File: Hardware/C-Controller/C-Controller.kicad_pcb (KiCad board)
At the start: 2 copper layers, 23 x 20 mm, 21 parts, among them J1 Conn_01x02, J2 Conn_01x04, J3 Conn_01x06, J4 Conn_01x07, J5 Conn_01x05, U1 STM32L031K6Tx

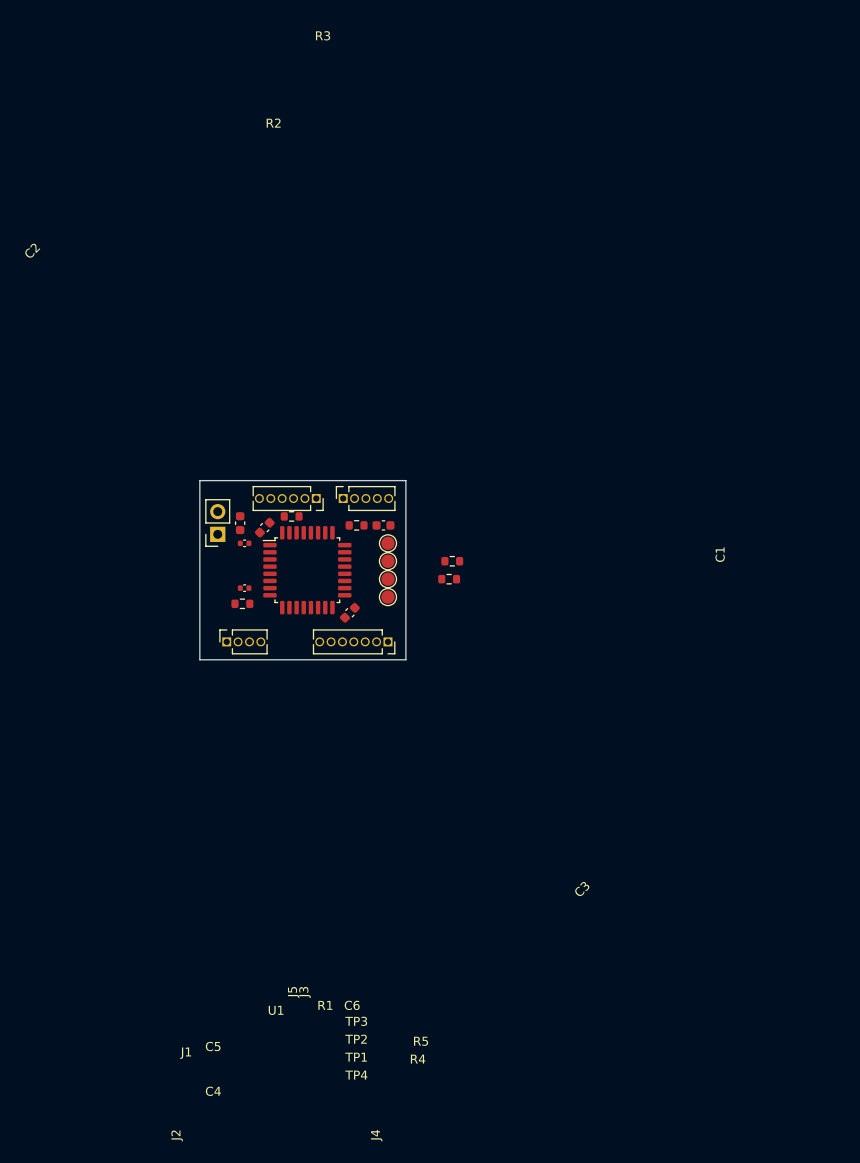
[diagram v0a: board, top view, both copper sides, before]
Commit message: 1mm pitch headers
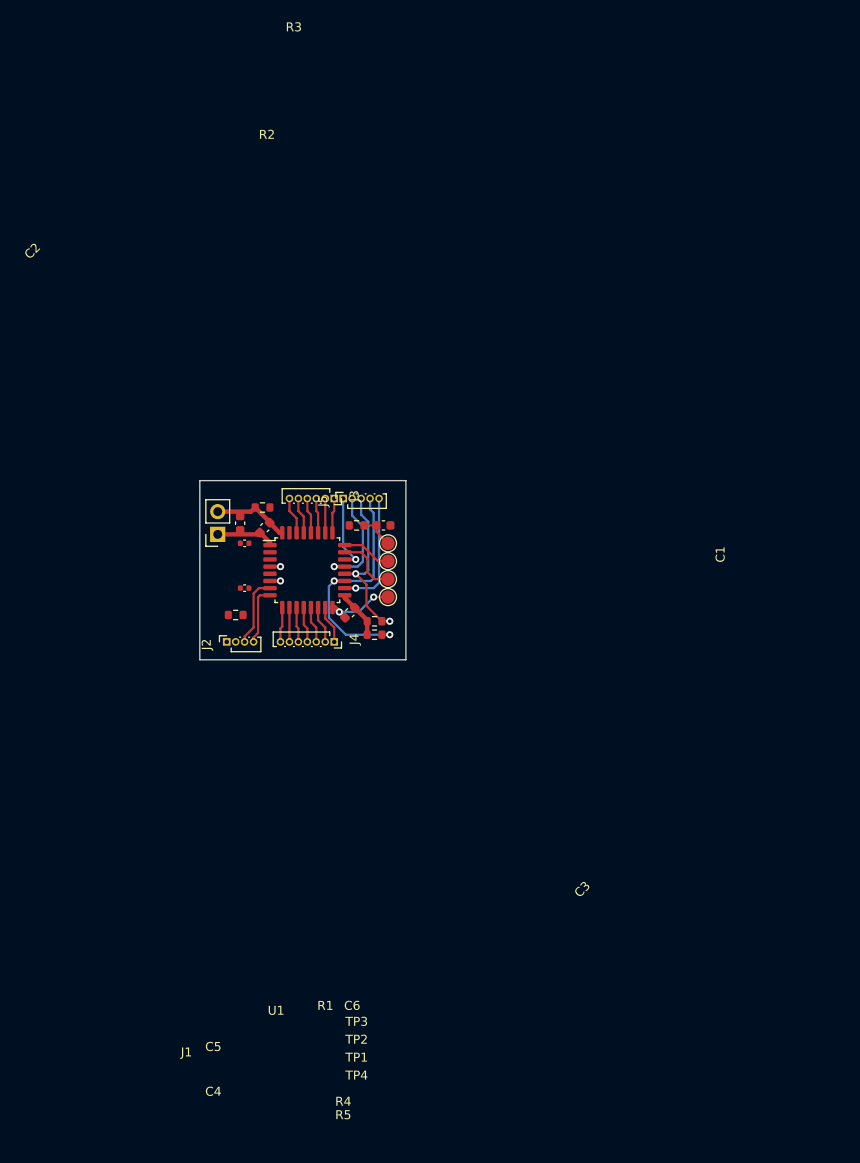
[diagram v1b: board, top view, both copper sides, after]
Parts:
- J2: footprint Connector_PinSocket_1.27mm:PinSocket_1x04_P1.27mm_Vertical -> Connector_PinSocket_1.00mm:PinSocket_1x04_P1.00mm_Vertical
- J3: footprint Connector_PinSocket_1.27mm:PinSocket_1x06_P1.27mm_Vertical -> Connector_PinSocket_1.00mm:PinSocket_1x06_P1.00mm_Vertical
- J4: footprint Connector_PinSocket_1.27mm:PinSocket_1x07_P1.27mm_Vertical -> Connector_PinSocket_1.00mm:PinSocket_1x07_P1.00mm_Vertical
- J5: footprint Connector_PinSocket_1.27mm:PinSocket_1x05_P1.27mm_Vertical -> Connector_PinSocket_1.00mm:PinSocket_1x05_P1.00mm_Vertical
- moved R5 11.9 mm to (127.5, 87.2)
- moved R4 9.56 mm to (127.5, 85.7)
- moved J4 6.00 mm to (123.0, 88.0)
- moved R3 3.40 mm to (115.0, 73.0)
- moved J3 2.00 mm to (123.0, 72.0)
- moved R2 1.46 mm to (112.0, 85.0)
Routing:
- net I2D1_SCL: track 0.00 -> 27.6 mm, vias 0 -> 2
- net I2C1_SDA: track 0.00 -> 18.5 mm, vias 0 -> 2
- net GND: track 0.00 -> 17.6 mm, vias 0 -> 2
- net PA8: track 0.00 -> 13.5 mm, vias 0 -> 1
- net PA11: track 0.00 -> 12.1 mm, vias 0 -> 1
- net +3V3: track 0.00 -> 11.9 mm
- net PA12: track 0.00 -> 8.60 mm, vias 0 -> 1
- net PA1: track 0.00 -> 7.89 mm
- net SYS_SWDIO: track 0.00 -> 6.95 mm
- net USART2_TX: track 0.00 -> 6.61 mm
- net SYS_SWCLK: track 0.00 -> 5.57 mm
- net RESET: track 0.00 -> 5.10 mm, vias 0 -> 1
- net PB1: track 0.00 -> 4.30 mm
- net PB7: track 0.00 -> 4.16 mm
- net PB0: track 0.00 -> 4.16 mm
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
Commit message: smaller components, crystal lib, status led, smaller board
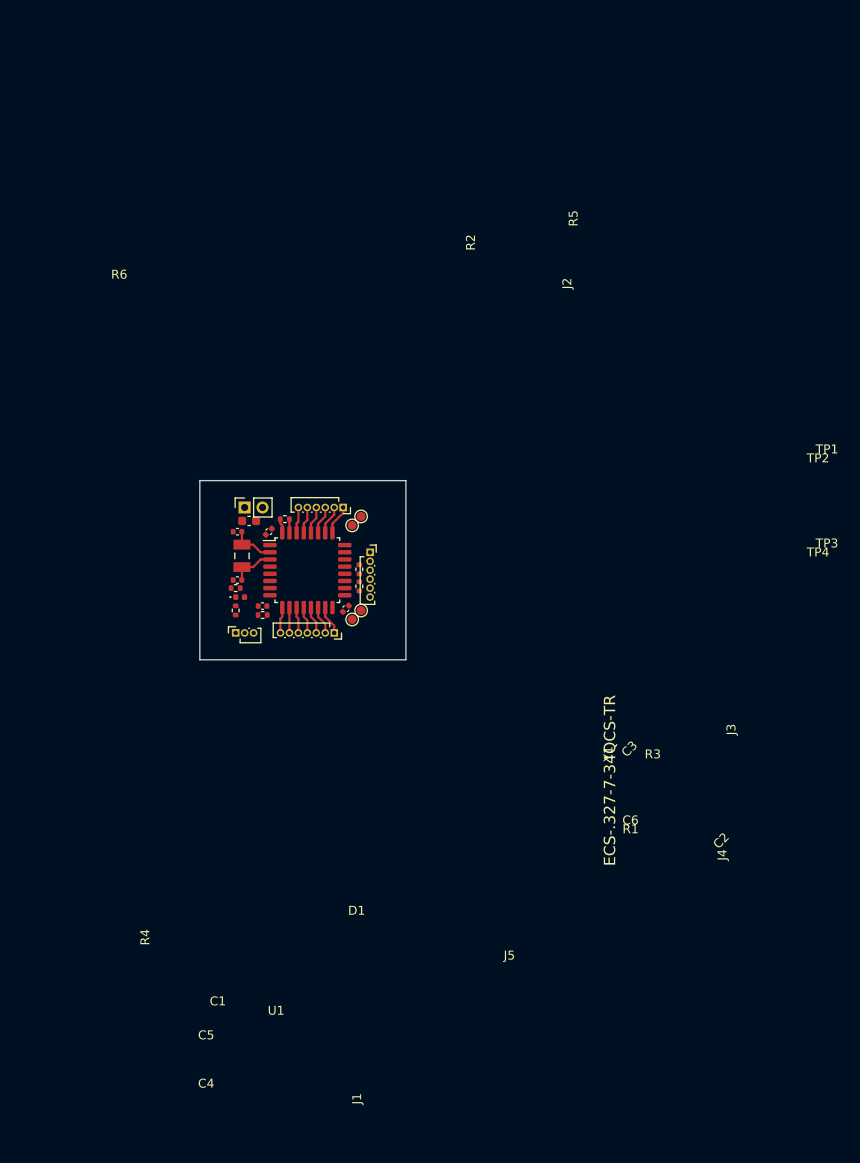
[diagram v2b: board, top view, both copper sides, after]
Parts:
- added D1: LED, LED_SMD:LED_0402_1005Metric, F.Cu at (112.5, 83.0)
- added R6: 1k, Resistor_SMD:R_0402_1005Metric, F.Cu at (112.0, 82.0)
- added Y1: ECS-.327-7-34QCS-TR, Crys_ECS Inc._ECS-.327-7-34QCS-TR:ECS_Inc.-ECX-34Q-0-0-0, F.Cu at (112.7, 78.4)
- C2, C3, C6: footprint Capacitor_SMD:C_0603_1608Metric -> Capacitor_SMD:C_0402_1005Metric
- J1: footprint Connector_PinSocket_2.54mm:PinSocket_1x02_P2.54mm_Vertical -> Connector_PinSocket_2.00mm:PinSocket_1x02_P2.00mm_Vertical
- J2: value Conn_01x04 -> Conn_01x03; footprint Connector_PinSocket_1.00mm:PinSocket_1x04_P1.00mm_Vertical -> Connector_PinSocket_1.00mm:PinSocket_1x03_P1.00mm_Vertical
- J5: value Conn_01x05 -> Conn_01x06; footprint Connector_PinSocket_1.00mm:PinSocket_1x05_P1.00mm_Vertical -> Connector_PinSocket_1.00mm:PinSocket_1x06_P1.00mm_Vertical
- R1, R2, R3, R4, R5: footprint Resistor_SMD:R_0603_1608Metric -> Resistor_SMD:R_0402_1005Metric
- TP1, TP2, TP3, TP4: footprint TestPoint:TestPoint_Pad_D1.5mm -> TestPoint:TestPoint_Pad_D1.0mm
- moved C6 16.2 mm to (115.0, 84.0)
- moved R1 14.5 mm to (115.0, 85.0)
- moved TP3 8.08 mm to (126.0, 84.5)
- moved TP1 7.62 mm to (126.0, 74.0)
- moved J5 6.71 mm to (127.0, 78.0), turned to 0 degrees
- moved R4 6.04 mm to (125.8, 79.9), turned to -90 degrees
- moved R5 5.66 mm to (125.8, 81.8), turned to 90 degrees
- moved TP2 5.66 mm to (125.0, 75.0)
- moved TP4 4.72 mm to (125.0, 85.5)
- moved J1 4.24 mm to (113.0, 73.0), turned to 90 degrees
- moved R3 2.81 mm to (117.5, 74.3)
- moved C5 1.53 mm to (112.2, 75.7)
- moved J2 1.41 mm to (112.0, 87.0)
- moved J3 1.41 mm to (124.0, 73.0)
- moved C4 1.20 mm to (112.2, 81.1)
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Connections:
- J2 pad 1: RESET -> SYS_WKUP1
- J2 pad 2: SYS_WKUP1 -> PA1
- J2 pad 3: PA1 -> USART2_TX
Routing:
- net I2D1_SCL: track 27.6 -> 0.00 mm, vias 2 -> 0
- net I2C1_SDA: track 18.5 -> 0.00 mm, vias 2 -> 0
- net GND: track 17.6 -> 1.62 mm, vias 2 -> 0
- net PA8: track 13.5 -> 0.00 mm, vias 1 -> 0
- net PA11: track 12.1 -> 0.00 mm, vias 1 -> 0
- net +3V3: track 11.9 -> 0.00 mm
- net PA12: track 8.60 -> 0.00 mm, vias 1 -> 0
- net PA1: track 7.89 -> 0.00 mm
- net SYS_SWDIO: track 6.95 -> 0.00 mm
- net USART2_TX: track 6.61 -> 0.00 mm
- net SYS_SWCLK: track 5.57 -> 0.00 mm
- net RESET: track 5.10 -> 0.00 mm, vias 1 -> 0
- net RCC_OSC32_IN: track 0.00 -> 4.94 mm
- net RCC_OSC32_OUT: track 0.00 -> 4.94 mm
- net BOOT: track 0.00 -> 1.53 mm
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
